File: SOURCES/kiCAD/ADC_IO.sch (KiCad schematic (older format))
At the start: 161 parts, among them IC2 PCM1808QPWRQ1, J1 Conn_01x08, J10 Conn_01x02, J11 Conn_Coaxial, J12 IDC_2x5, J3 Conn_01x08, J5 MJ-519, J6 8P_DIP_SOCKET, J9 Conn_01x02, Q12 MJD45H11T4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

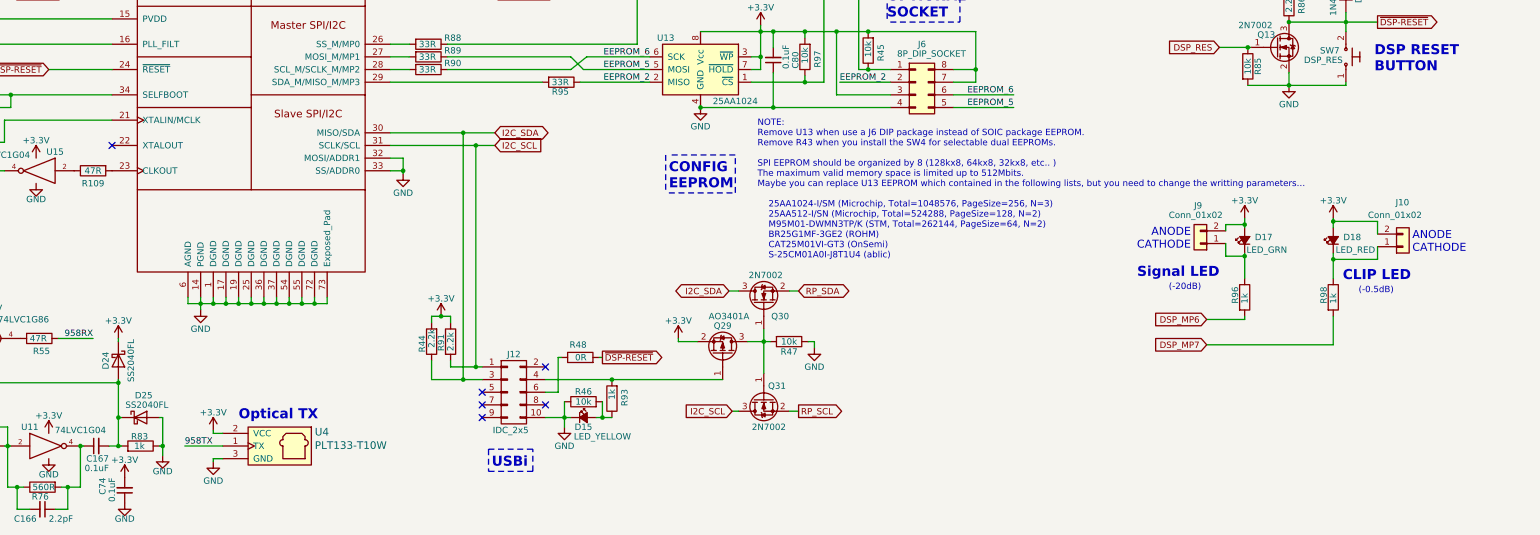
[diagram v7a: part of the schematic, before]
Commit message: Voltage Regulator Changed to LM317
PCB layout is also updated in some of the places.
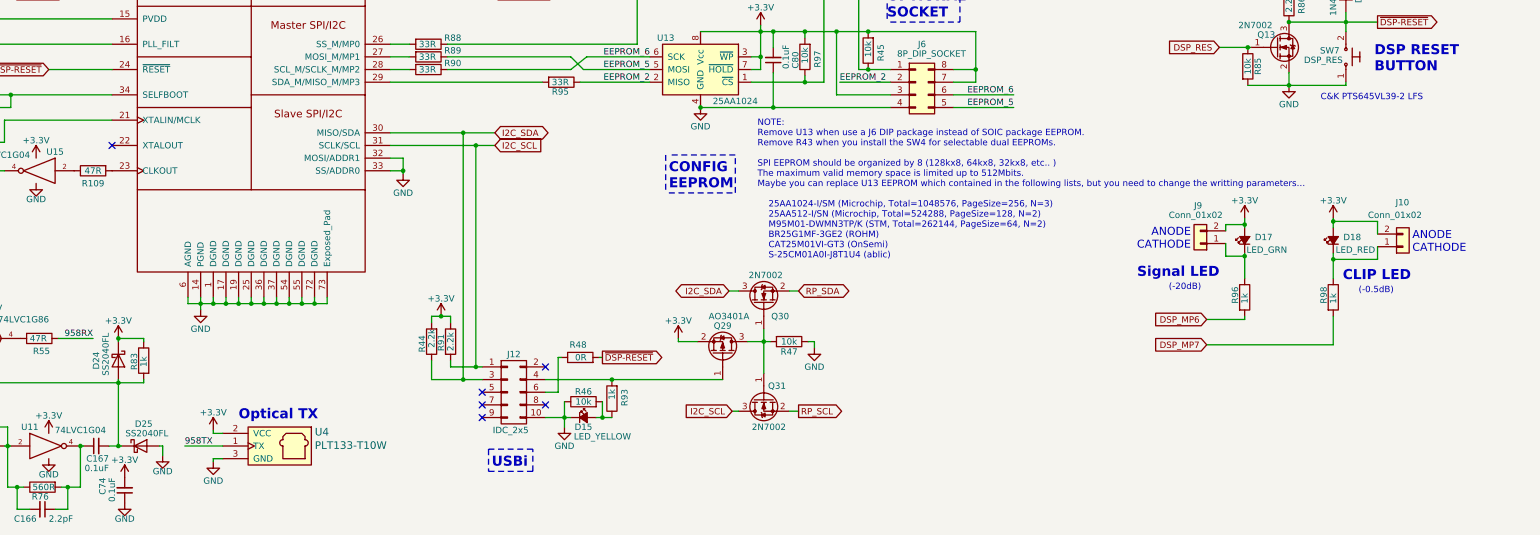
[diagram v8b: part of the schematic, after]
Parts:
- C31: footprint Capacitor_SMD:C_0805_2012Metric_Pad1.18x1.45mm_HandSolder -> Capacitor_SMD:C_0603_1608Metric_Pad1.08x0.95mm_HandSolder; JLPCB# C49678 -> C14663
- C36, C51: Description (none) -> PLL Loop FIlter Snabber Cap
- C56: Description (none) -> PLL Loop FIlter Cap (C0G will better)
- C66: Description (none) -> Prepared for just in case
- D15: Description (none) -> Indicator for USBi is Active
- D17, D18: Description Remove this if you use extension header -> Remove this if you use LED extension header
- IC2: Description 99dB SNR is only for 48kHz Sampling -> ADC 99dB SNR is only available @48kHz Sampling
- J11: Description RCA-pin Input Connector -> RCA-pin Input Connector(Yellow)CUI RCJ-044
- J12: Description for USBi -> 10pin IDC header for USBi
- J5: Description (none) -> Vertical Stereo RCA-pin Jack (Upper=Left, Lower=Right) RCJ-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
- J6: Description Just for the Altanative choice of EEPROM package -> Just Prepared for the Altanative choice of EEPROM package
- SW4: Description (none) -> Optional Program EEPROM A/B Select switch
- T1: Description Audio Transformers / Signal Transformers THT Digital Audio 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 -> S/PDIF Transformer THT Digital-Audio 2500uH 1-Port
- U10: Description (none) -> EXOR for Maerge S/PDIF Signals
- U11, U15: Description (none) -> for Coax S/PDIF Input Amp
- U12: Description (none) -> SigmaDSP
- U13: Description (none) -> Might be substitute with 256Mbit/512Mbit SPI EEPROM
- U2: Description (none) -> Optical S/PDIF RX (max. 16Mbps)
- U4: Description (none) -> Optical S/PDIF TX (max. 16Mbps)
- Y1: Description 50MHz TCXO 1.6 to 3.63 Volts -> 24.576MHz or 22.5792MHz TCXO 1.6 to 3.63 Volts
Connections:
- net +3V3: now also R83.1
- net GND: no longer R83.1
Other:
- note added: "C&K PTS645VL39-2 LFS"
- moved on the sheet: D25, R83
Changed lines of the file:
@@
 Title "FreeDSP OCTAVIA ADC/DSP Part"
 Date "2023-08-14"
-Rev "0.32"
+Rev "0.33"
 Comp ""
 Comment1 ""
@@
 F 3 " ~" H 1425 1650 50  0001 C CNN
 F 4 "HAND" H 1425 1750 50  0001 C CNN "JLPCB#"
+F 5 "Vertical Stereo RCA-pin Jack (Upper=Left, Lower=Right) RCJ-2232,RCJ-2233" H 1425 1750 50  0001 C CNN "Description"
 	1    1425 1750
 	-1   0    0    -1
@@
 F 2 "Myfootprints:PCM1808QPWRQ1" H 6350 625 50  0001 C CNN
 F 3 "http://www.ti.com/lit/ds/symlink/pcm1808-q1.pdf" H 6350 525 50  0001 C CNN
-F 4 "99dB SNR is only for 48kHz Sampling" H 6350 425 50  0001 C CNN "Description"
+F 4 "ADC 99dB SNR is only available @48kHz Sampling" H 6350 425 50  0001 C CNN "Description"
 F 5 "RS" H 6350 325 50  0001 C CNN "Supplier_Name"
 F 6 "" H 6350 225 50  0001 C CNN "RS Part Number"
@@
 F 0 "C31" H 6050 1075 50  0000 L CNN
 F 1 "0.1uF" V 6150 1175 50  0000 L CNN
-F 2 "Capacitor_SMD:C_0805_2012Metric_Pad1.18x1.45mm_HandSolder" H 6050 1275 50  0001 C CNN
+F 2 "Capacitor_SMD:C_0603_1608Metric_Pad1.08x0.95mm_HandSolder" H 6050 1275 50  0001 C CNN
 F 3 "" H 6050 1275 50  0001 C CNN
-F 4 "C49678" H 6050 1275 50  0001 C CNN "JLPCB#"
+F 4 "C14663" H 6050 1275 50  0001 C CNN "JLPCB#"
 	1    6050 1275
 	1    0    0    1
@@
 F 3 "" H 5325 10625 60  0000 C CNN
 F 4 "HAND" H 5325 10625 50  0001 C CNN "JLPCB#"
+F 5 "Optical S/PDIF TX (max. 16Mbps)" H 5325 10625 50  0001 C CNN "Description"
 	1    5325 10625
 	-1   0    0    -1
@@
 F 3 "~" H 2275 7200 50  0001 C CNN
 F 4 "C1744" H 2275 7200 50  0001 C CNN "JLPCB#"
+F 5 "PLL Loop FIlter Snabber Cap" H 2275 7200 50  0001 C CNN "Description"
 	1    2275 7200
 	-1   0    0    1
@@
 F 3 "" H 1500 9725 60  0000 C CNN
 F 4 "HAND" H 1500 9725 50  0001 C CNN "JLPCB#"
+F 5 "Optical S/PDIF RX (max. 16Mbps)" H 1500 9725 50  0001 C CNN "Description"
 	1    1500 9725
 	1    0    0    -1
@@
 F 3 "" H 5100 7900 60  0000 C CNN
 F 4 "C654402" H 5100 6300 50  0001 C CNN "JLPCB#"
+F 5 "SigmaDSP " H 5100 6300 50  0001 C CNN "Description"
 	1    5100 6300
 	1    0    0    -1
@@
 F 3 "~" H 2075 7200 50  0001 C CNN
 F 4 "C46653" H 2075 7200 50  0001 C CNN "JLPCB#"
+F 5 "PLL Loop FIlter Snabber Cap" H 2075 7200 50  0001 C CNN "Description"
 	1    2075 7200
 	-1   0    0    1
@@
 F 3 "~" H 2575 7200 50  0001 C CNN
 F 4 "C1716" H 2575 7200 50  0001 C CNN "JLPCB#"
+F 5 "PLL Loop FIlter Cap (C0G will better)" H 2575 7200 50  0001 C CNN "Description"
 	1    2575 7200
 	-1   0    0    1
@@
 F 2 "Crystals:Crystal_SMD_TXC_7M-4pin_3.2x2.5mm_HandSoldering" H 1525 7725 50  0001 C CNN
 F 3 "http://www.kyocera.co.jp/prdct/electro/pdf/clock_k_j.pdf" H 1525 7625 50  0001 C CNN
-F 4 "50MHz TCXO 1.6 to 3.63 Volts" H 1525 7525 50  0001 C CNN "Description"
+F 4 "24.576MHz or 22.5792MHz TCXO 1.6 to 3.63 Volts" H 1525 7525 50  0001 C CNN "Description"
 F 5 "RS" H 1525 7425 50  0001 C CNN "Supplier_Name"
 F 6 "" H 1525 7325 50  0001 C CNN "RS Part Number"
@@
 F 3 "http://ww1.microchip.com/downloads/en/DeviceDoc/21832H.pdf" H 8625 7900 50  0001 C CNN
 F 4 "C157455" H 8650 7500 50  0001 C CNN "JLPCB#"
+F 5 "Might be substitute with 256Mbit/512Mbit SPI EEPROM" H 8650 7500 50  0001 C CNN "Description"
 	1    8650 7500
 	-1   0    0    -1
@@
 F 3 "" H 7175 8850 60  0000 C CNN
 F 4 "HAND" H 7175 10050 50  0001 C CNN "JLPCB#"
-F 5 "for USBi" H 7175 10050 50  0001 C CNN "Description"
+F 5 "10pin IDC header for USBi" H 7175 10050 50  0001 C CNN "Description"
 	1    7175 10050
 	1    0    0    -1
@@
 F 3 "" V 7725 10250 60  0000 C CNN
 F 4 "C72038" H 7725 10250 50  0001 C CNN "JLPCB#"
+F 5 "Indicator for USBi is Active" H 7725 10250 50  0001 C CNN "Description"
 	1    7725 10250
 	1    0    0    -1
@@
 F 3 " ~" H 1250 10475 50  0001 C CNN
 F 4 "HAND" H 1250 10475 50  0001 C CNN "JLPCB#"
-F 5 "RCA-pin Input Connector" H 1250 10475 50  0001 C CNN "Description"
+F 5 "RCA-pin Input Connector(Yellow)CUI RCJ-044" H 1250 10475 50  0001 C CNN "Description"
 	1    1250 10475
 	-1   0    0    -1
@@
 F 2 "MyLibrary:PE65612NL" H 2200 10575 50  0001 L CNN
 F 3 "https://componentsearchengine.com/Datasheets/1/PE-65612NL.pdf" H 2200 10475 50  0001 L CNN
-F 4 "Audio Transformers / Signal Transformers THT Digital Audio 2500uH 1-Port" H 2200 10375 50  0001 L CNN "Description"
+F 4 "S/PDIF Transformer THT Digital-Audio 2500uH 1-Port" H 2200 10375 50  0001 L CNN "Description"
 F 5 "6.6" H 2200 10275 50  0001 L CNN "Height"
 F 6 "Pulse" H 2200 10175 50  0001 L CNN "Manufacturer_Name"
@@
 F 3 "~" H 3000 10325 50  0001 C CNN
 F 4 "NOP" H 3000 10325 50  0001 C CNN "JLPCB#"
+F 5 "Prepared for just in case" H 3000 10325 50  0001 C CNN "Description"
 	1    3000 10325
 	0    -1   1    0
@@
 F 3 "http://www.ti.com/lit/sg/scyt129e/scyt129e.pdf" H 3500 10475 50  0001 C CNN
 F 4 "C434067" H 3500 10475 50  0001 C CNN "JLPCB#"
+F 5 "for Coax S/PDIF Input Amp" H 3500 10475 50  0001 C CNN "Description"
 	1    3500 10475
 	1    0    0    -1
@@
 F 3 "http://www.ti.com/lit/sg/scyt129e/scyt129e.pdf" H 3025 9625 50  0001 C CNN
 F 4 "C73458" H 3025 9625 50  0001 C CNN "JLPCB#"
+F 5 "EXOR for Maerge S/PDIF Signals" H 3025 9625 50  0001 C CNN "Description"
 	1    3025 9625
 	1    0    0    -1
@@
 L Device:R R?
 U 1 1 68A3A234
-P 4225 10475
+P 4250 9800
 AR Path="/5D67FDC6/68A3A234" Ref="R?"  Part="1"
 AR Path="/68A3A234" Ref="R?"  Part="1"
 AR Path="/5D902CF8/68A3A234" Ref="R83"  Part="1"
-F 0 "R83" V 4300 10400 50  0000 L CNN
-F 1 "1k" V 4225 10425 50  0000 L CNN
-F 2 "Resistor_SMD:R_0603_1608Metric" V 4155 10475 50  0001 C CNN
-F 3 "~" H 4225 10475 50  0001 C CNN
-F 4 "C21190" H 4225 10475 50  0001 C CNN "JLPCB#"
-	1    4225 10475
-	0    1    -1   0
+F 0 "R83" V 4325 9725 50  0000 L CNN
+F 1 "1k" V 4250 9750 50  0000 L CNN
+F 2 "Resistor_SMD:R_0603_1608Metric" V 4180 9800 50  0001 C CNN
+F 3 "~" H 4250 9800 50  0001 C CNN
+F 4 "C21190" H 4250 9800 50  0001 C CNN "JLPCB#"
+	1    4250 9800
+	-1   0    0    -1
 $EndComp
 Wire Wire Line
@@
 F 3 "" V 13650 8850 60  0000 C CNN
 F 4 "C2286" H 13650 8850 50  0001 C CNN "JLPCB#"
-F 5 "Remove this if you use extension header" H 13650 8850 50  0001 C CNN "Description"
+F 5 "Remove this if you use LED extension header" H 13650 8850 50  0001 C CNN "Description"
 	1    13650 8850
 	0    -1   -1   0
@@
 F 3 "" V 12950 8850 60  0000 C CNN
 F 4 "C72043" H 12950 8850 50  0001 C CNN "JLPCB#"
-F 5 "Remove this if you use extension header" H 12950 8850 50  0001 C CNN "Description"
+F 5 "Remove this if you use LED extension header" H 12950 8850 50  0001 C CNN "Description"
 	1    12950 8850
 	0    -1   -1   0
@@
 F 3 "http://www.ti.com/lit/sg/scyt129e/scyt129e.pdf" H 3400 8300 50  0001 C CNN
 F 4 "C434067" H 3400 8300 50  0001 C CNN "JLPCB#"
+F 5 "for Coax S/PDIF Input Amp" H 3400 8300 50  0001 C CNN "Description"
 	1    3400 8300
 	-1   0    0    -1
@@
 F 3 "~" H 10350 7600 50  0001 C CNN
 F 4 "NOP" H 10350 7600 50  0001 C CNN "JLPCB#"
-F 5 "Just for the Altanative choice of EEPROM package" H 10350 7600 50  0001 C CNN "Description"
+F 5 "Just Prepared for the Altanative choice of EEPROM package" H 10350 7600 50  0001 C CNN "Description"
 	1    10350 7600
 	1    0    0    -1
@@
 F 3 "~" H 9325 6575 50  0001 C CNN
 F 4 "NOP" H 9325 6375 50  0001 C CNN "JLPCB#"
+F 5 "Optional Program EEPROM A/B Select switch" H 9325 6375 50  0001 C CNN "Description"
 	1    9325 6375
 	1    0    0    1
@@
 Wire Wire Line
 	3975 10475 4050 10475
-Wire Wire Line
-	4050 9975 4050 10250
 Connection ~ 4050 10475
 Wire Wire Line
@@
 AR Path="/652CCFB7" Ref="D?"  Part="1"
 AR Path="/5D902CF8/652CCFB7" Ref="D24"  Part="1"
-F 0 "D24" H 4050 9700 50  0000 C CNN
-F 1 "SS2040FL" H 4050 9900 50  0000 C CNN
+F 0 "D24" H 4050 9625 50  0000 C CNN
+F 1 "SS2040FL" H 4000 9700 50  0000 C CNN
 F 2 "Diode_SMD:D_SOD-123" H 4050 9625 50  0001 C CNN
 F 3 "http://www.vishay.com/docs/85660/bat42.pdf" H 4050 9800 50  0001 C CNN
@@
 L Diode:BAT43W-V D?
 U 1 1 654BDB82
-P 4225 10250
+P 4225 10475
 AR Path="/5D60B524/654BDB82" Ref="D?"  Part="1"
 AR Path="/654BDB82" Ref="D?"  Part="1"
 AR Path="/5D902CF8/654BDB82" Ref="D25"  Part="1"
-F 0 "D25" H 4250 10425 50  0000 C CNN
-F 1 "SS2040FL" H 4275 10350 50  0000 C CNN
-F 2 "Diode_SMD:D_SOD-123" H 4225 10075 50  0001 C CNN
-F 3 "http://www.vishay.com/docs/85660/bat42.pdf" H 4225 10250 50  0001 C CNN
-F 4 "C8598" H 4225 10250 50  0001 C CNN "JLPCB#"
-	1    4225 10250
+F 0 "D25" H 4250 10650 50  0000 C CNN
+F 1 "SS2040FL" H 4275 10575 50  0000 C CNN
+F 2 "Diode_SMD:D_SOD-123" H 4225 10300 50  0001 C CNN
+F 3 "http://www.vishay.com/docs/85660/bat42.pdf" H 4225 10475 50  0001 C CNN
+F 4 "C8598" H 4225 10475 50  0001 C CNN "JLPCB#"
+	1    4225 10475
 	1    0    0    -1
 $EndComp
-Wire Wire Line
-	4075 10250 4050 10250
-Connection ~ 4050 10250
-Wire Wire Line
-	4050 10250 4050 10475
-Wire Wire Line
-	4400 10475 4400 10250
-Wire Wire Line
-	4400 10250 4375 10250
-Connection ~ 4400 10475
 $Comp
 L Device:C_Small C?
@@
 Text Notes 7925 6475 0    50   ~ 0
 (Optional  Dual ROM A/B Switch)
+Wire Wire Line
+	4050 9975 4050 10475
+Wire Wire Line
+	4250 9625 4050 9625
+Wire Wire Line
+	4250 9625 4250 9650
+Connection ~ 4050 9625
+Wire Wire Line
+	4250 9950 4250 9975
+Wire Wire Line
+	4250 9975 4050 9975
+Text Notes 13550 7750 0    50   ~ 0
+C&K PTS645VL39-2 LFS
 $EndSCHEMATC
